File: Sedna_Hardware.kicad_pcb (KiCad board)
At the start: 2 copper layers, 51 parts, among them J1 PJ-102A, J10 5-103634-2, J11 2-644488-2, J2 61201021721, J3 PPTC141LFBN-RC, J4 0878340619, J5 2-644803-3, J6 2-644488-3, J7 1935161, J8 1935161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

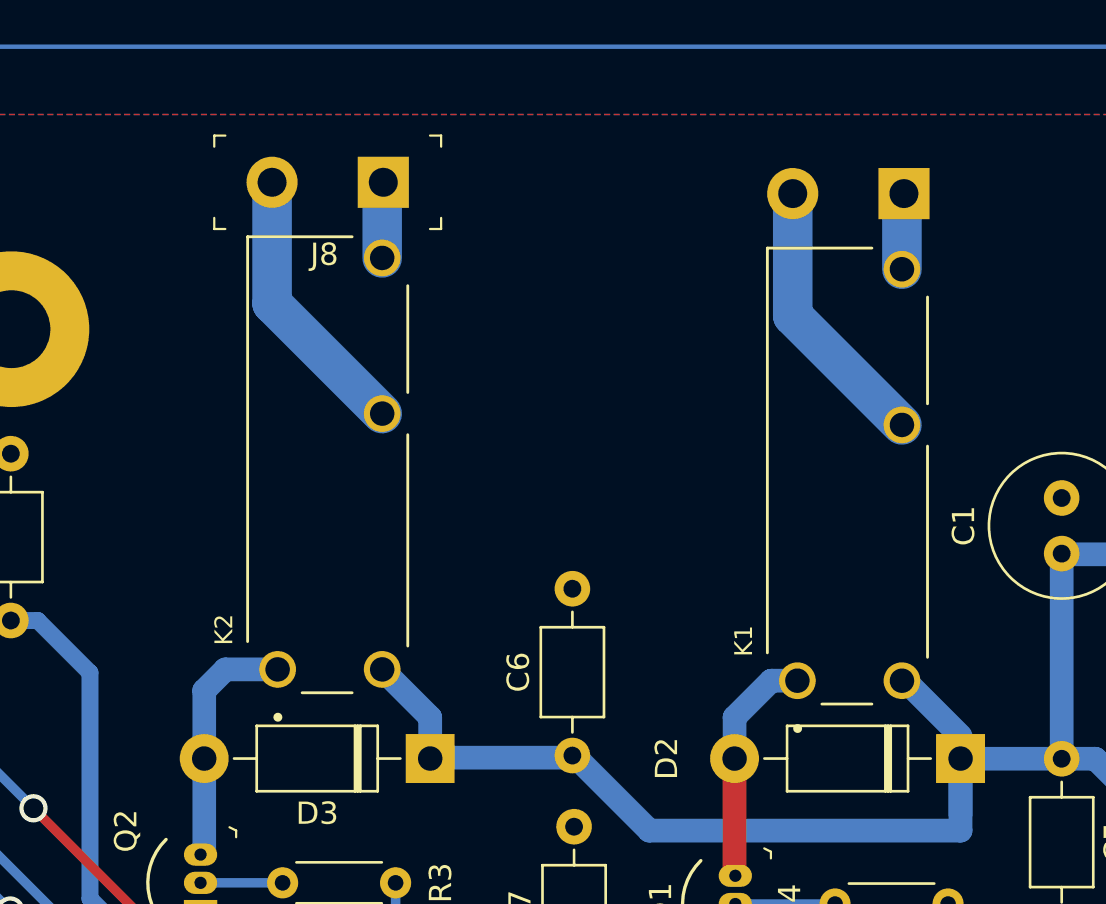
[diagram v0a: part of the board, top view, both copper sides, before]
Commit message: modified relay due to stock issues
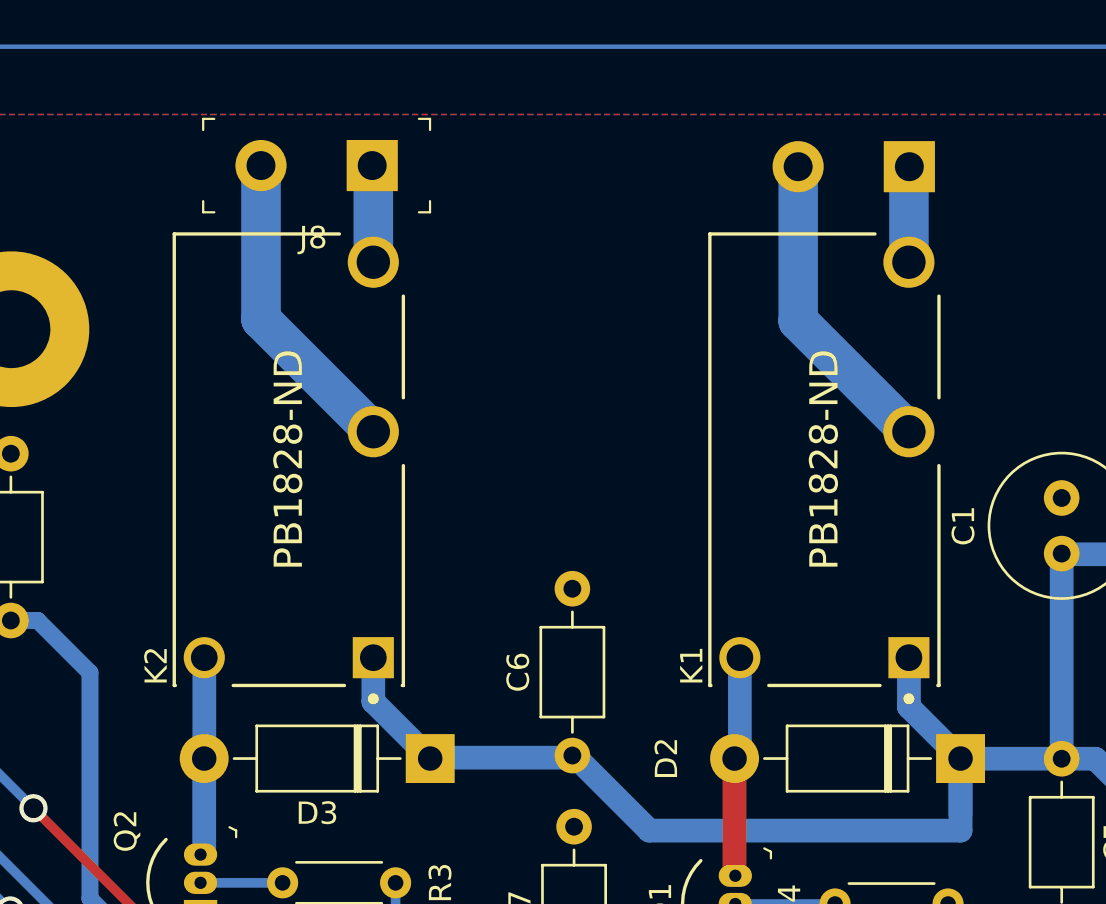
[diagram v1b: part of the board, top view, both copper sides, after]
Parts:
- K1, K2: value ALDP105W -> PB1828-ND; footprint ALDP105W:RELAY_ALDP105W -> eec:TE_Connectivity-1461352-2-MFG
- moved K2 1.76 mm to (128.3, 72.9)
- moved K1 1.27 mm to (152.4, 72.9)
- moved J7 1.23 mm to (156.2, 59.8)
- moved J8 0.90 mm to (132.1, 59.7)
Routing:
- net Net-(D3-Pad2): track 10.9 -> 8.69 mm
- net Net-(J8-Pad2): track 12.5 -> 14.1 mm
- net Net-(J7-Pad2): track 12.4 -> 14.0 mm
- net +5V: track 101.6 -> 102.9 mm
- net Net-(J8-Pad1): track 3.42 -> 4.37 mm
- net Net-(J7-Pad1): track 3.44 -> 4.30 mm

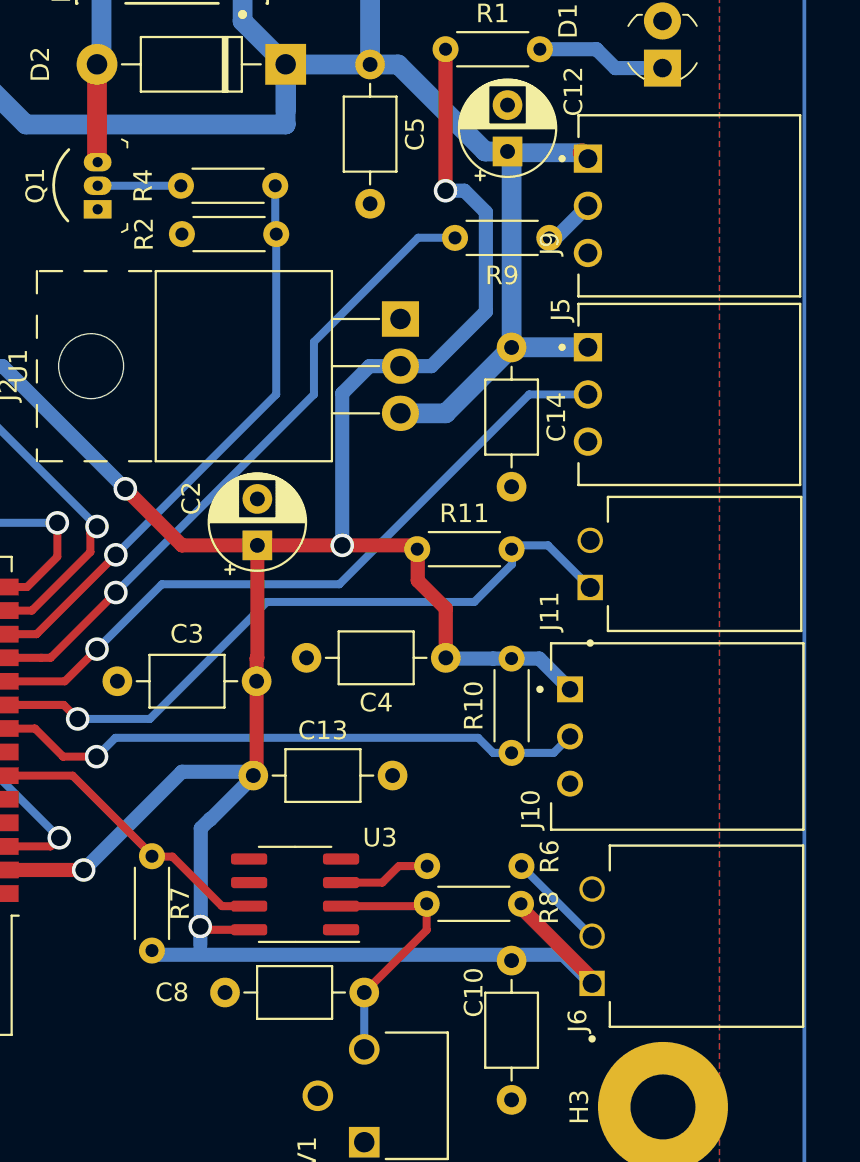
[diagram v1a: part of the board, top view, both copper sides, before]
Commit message: placed new header's footpring
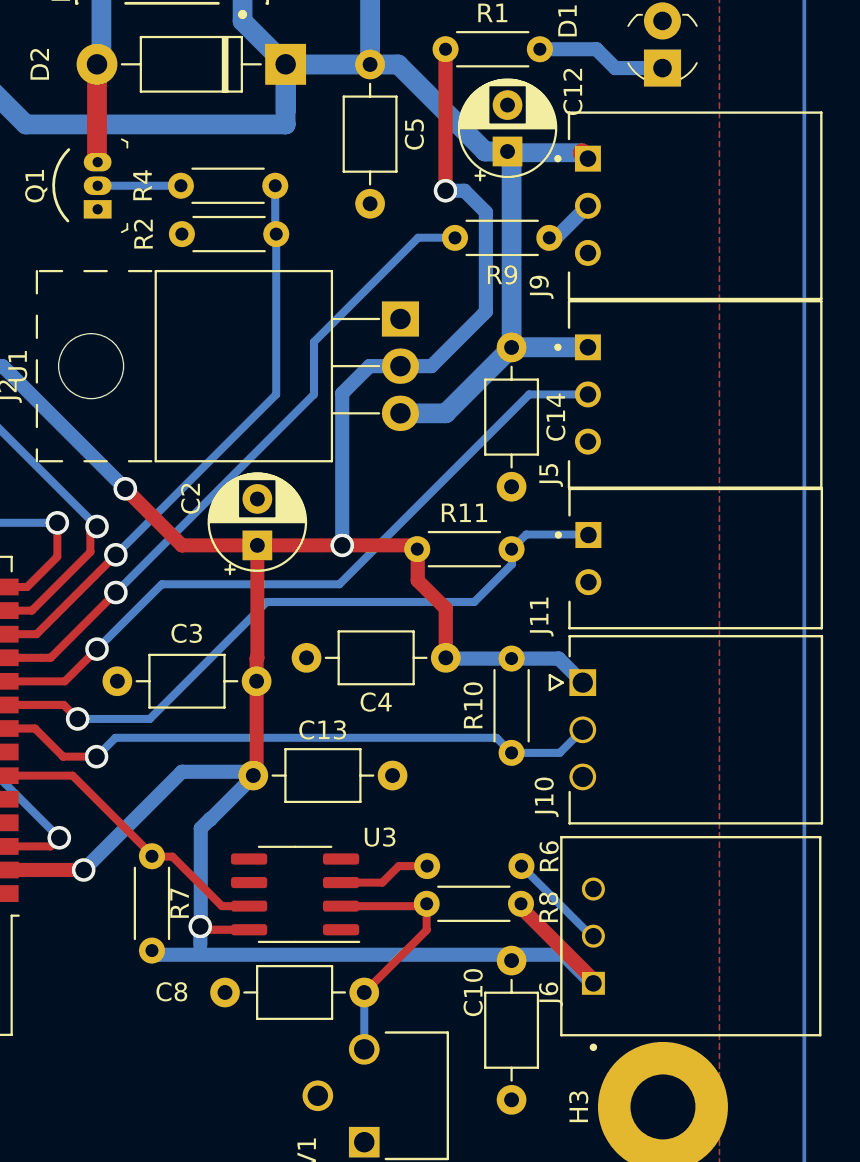
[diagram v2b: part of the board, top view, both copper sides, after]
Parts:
- J10: value 5-103634-2 -> 5-103735-2; footprint 5-103634-2:TE_5-103634-2 -> 5-103735-2:MOLEX_1719740003
- J11: value 2-644488-2 -> 5-103634-1; footprint 2-644488-2:TE_2-644488-2 -> 2-103634-9:TE_2-103634-9
- J5, J9: value 2-644803-3 -> 5-103634-2; footprint 2-644803-3:TE_2-644803-3 -> 5-103634-2:TE_5-103634-2
- J6: value 2-644488-3 -> 5-103361-1; footprint 2-644488-3:TE_2-644488-3 -> 5-103361-1:TE_5-103361-1
- moved J10 2.98 mm to (174.5, 119.7), turned to 90 degrees
- moved J11 1.56 mm to (174.8, 113.0), turned to -90 degrees
- moved J6 0.07 mm to (175.1, 135.9)
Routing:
- net TEMP_SEN_IN: track 32.4 -> 33.3 mm
- net FLOAT_SEN_IN: track 37.5 -> 36.8 mm
- net +3V3: track 263.2 -> 263.7 mm

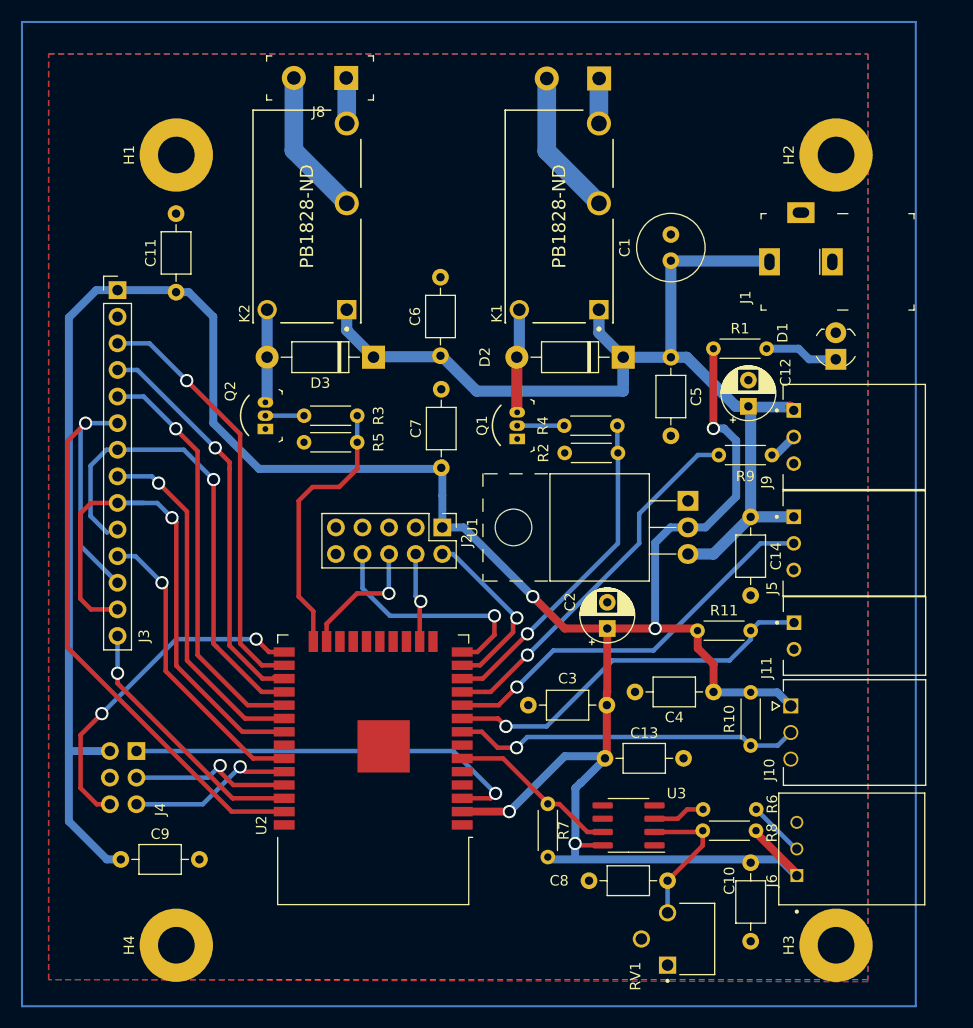
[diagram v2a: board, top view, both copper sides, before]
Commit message: Edit PCB making pads bigger
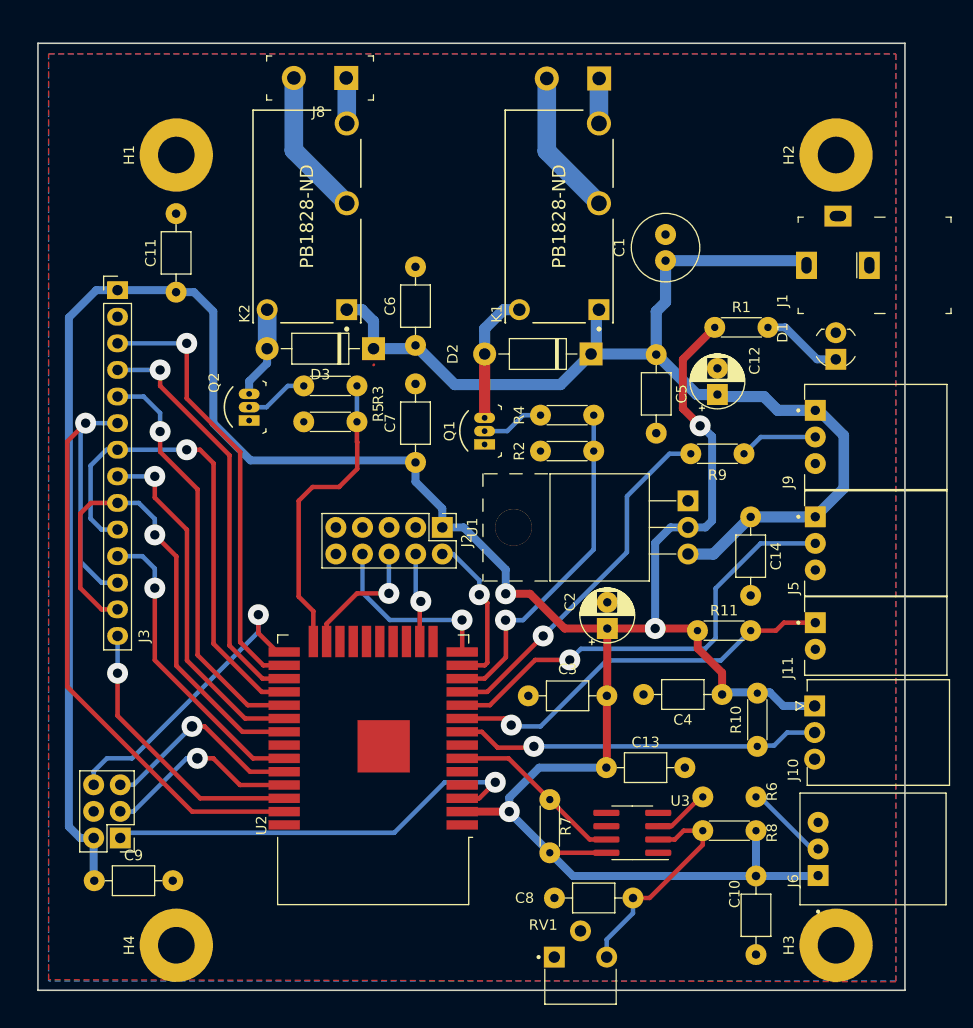
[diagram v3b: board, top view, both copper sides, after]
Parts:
- J4: moved to F.Cu
- moved RV1 9.71 mm to (154.4, 144.6), turned to 0 degrees
- moved J4 8.45 mm to (110.5, 132.3)
- moved C8 3.69 mm to (159.4, 138.0)
- moved J1 3.55 mm to (179.0, 77.6)
- moved C9 3.25 mm to (108.0, 136.3)
- moved C12 3.16 mm to (167.5, 89.9)
- moved Q1 3.16 mm to (145.3, 94.7)
- moved D2 3.09 mm to (155.4, 86.1)
- moved R5 2.84 mm to (133.1, 89.1)
- moved R9 2.67 mm to (165.0, 95.6)
- moved C6 2.58 mm to (138.7, 85.2)
- moved C7 2.51 mm to (138.7, 96.4)
- moved R4 2.47 mm to (155.7, 91.9)
- moved R2 2.32 mm to (150.6, 95.3)
- moved J10 2.27 mm to (176.8, 119.7)
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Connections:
- J2 pad 2: JTAG_TMS -> RELAY_CTRL_1
- U2 pad 13: JTAG_TMS -> RELAY_CTRL_1
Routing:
- net JTAG_TMS: track 17.5 -> 0.00 mm, vias 1 -> 0
- net RELAY_CTRL_1: track 31.4 -> 48.0 mm, vias 1 -> 2
- net Net-(C8-Pad1): track 14.5 -> 21.6 mm
- net JTAG_TDI: track 22.5 -> 17.3 mm
- net LED_STRIP_CTRL: track 38.1 -> 42.9 mm
- net Net-(J9-Pad2): track 3.08 -> 7.47 mm
- net +5V: track 102.9 -> 107.3 mm
- net MISO_LCD: track 52.0 -> 47.9 mm
- net PROG_RXD0: track 15.8 -> 19.7 mm
- net PROG_IO0: track 33.2 -> 30.1 mm, vias 2 -> 1
- net MOSI_LCD: track 69.3 -> 72.4 mm
- net PROG_TXD0: track 15.7 -> 18.8 mm
- net RELAY_CTRL_2: track 25.9 -> 28.8 mm
- net Net-(J6-Pad2): track 5.37 -> 7.99 mm
- net PROG_EN: track 39.3 -> 41.8 mm
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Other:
- board outline added: 82.8 x 90.4 mm
